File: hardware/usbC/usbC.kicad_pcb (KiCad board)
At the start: 2 copper layers, 27.5 x 25.6 mm, 17 parts, among them J2 Conn_01x02, J3 Conn_01x02, J4 Conn_01x01, J5 Conn_01x02, J6 Conn_01x01, J7 Conn_01x01, J8 Conn_01x01, J9 Connector, USB-TYPE-C-16P, U1 USBLC6-2SC6, U2 AMS1117-3.3

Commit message: wip
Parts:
- removed J4, J8: Conn_01x01, Connector_PinHeader_1.00mm:PinHeader_1x01_P1.00mm_Vertical
- added J1: Conn_01x02, LIB_S2B-ZR_LF__SN_:S2BZRLFSN, F.Cu at (93.0, 83.0)
- J6, J7: value Conn_01x01 -> Conn_01x02; footprint Connector_PinHeader_1.00mm:PinHeader_1x01_P1.00mm_Vertical -> Connector_PinHeader_2.54mm:PinHeader_1x02_P2.54mm_Vertical
- moved J6 24.7 mm to (119.0, 78.7)
- moved J7 12.5 mm to (103.5, 75.5)
- moved J5 7.07 mm to (100.0, 83.0)
- moved J2 2.23 mm to (94.8, 71.1), turned to 180 degrees
- moved C18 1.58 mm to (100.0, 68.3), turned to 90 degrees
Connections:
- F1 pad 1: Net-(F1-Pad1) -> Net-(J7-Pin_2)
- J6 pad 1: GND -> /D+
- J9 pad A9B4: Net-(F1-Pad1) -> Net-(J7-Pin_2)
- J9 pad B9A4: Net-(F1-Pad1) -> Net-(J7-Pin_2)
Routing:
- net VCC: track 16.9 -> 38.6 mm
- net Net-(J7-Pin_2): track 0.00 -> 17.6 mm
- net GND: track 60.2 -> 46.9 mm, vias 8 -> 10
- net Net-(F1-Pad1): track 11.4 -> 0.00 mm
- net /D-: track 9.26 -> 16.3 mm
- net /D+: track 13.1 -> 17.2 mm
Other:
- board size 27.5 x 25.6 mm -> 32 x 25.6 mm

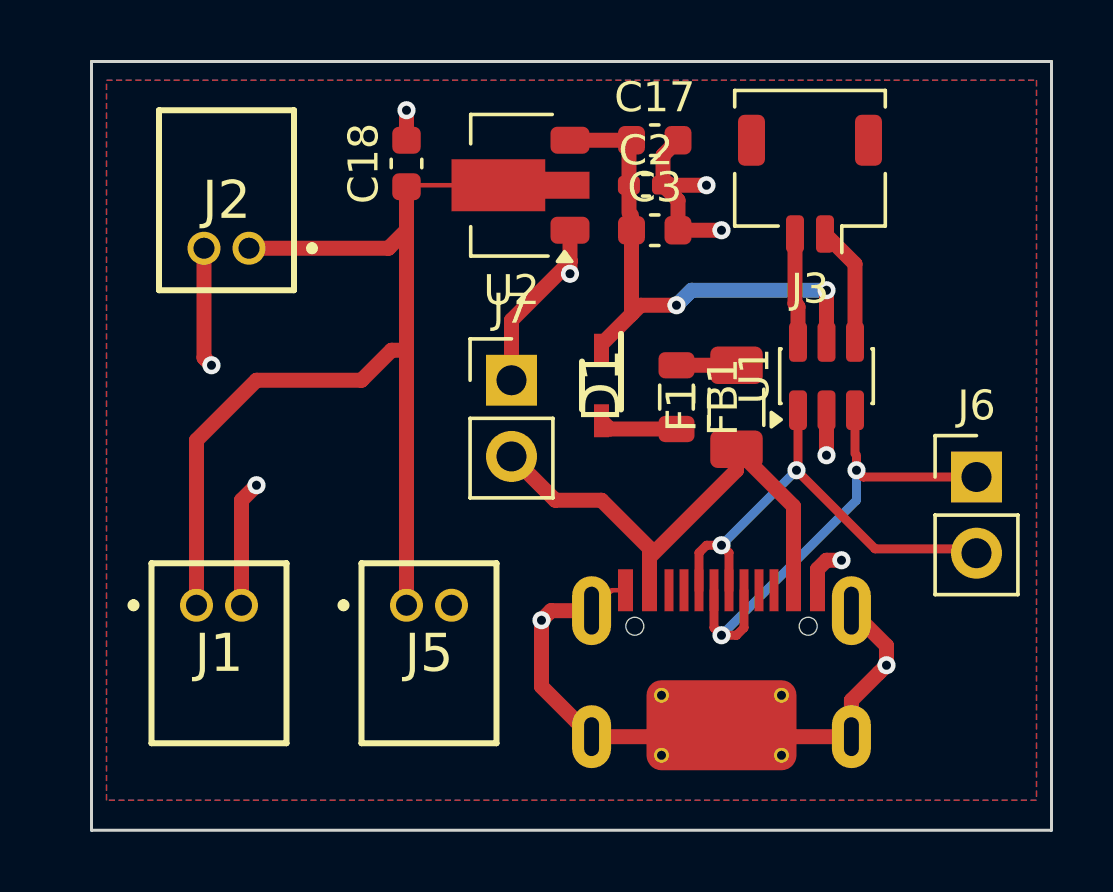
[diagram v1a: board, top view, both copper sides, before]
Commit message: usbc production
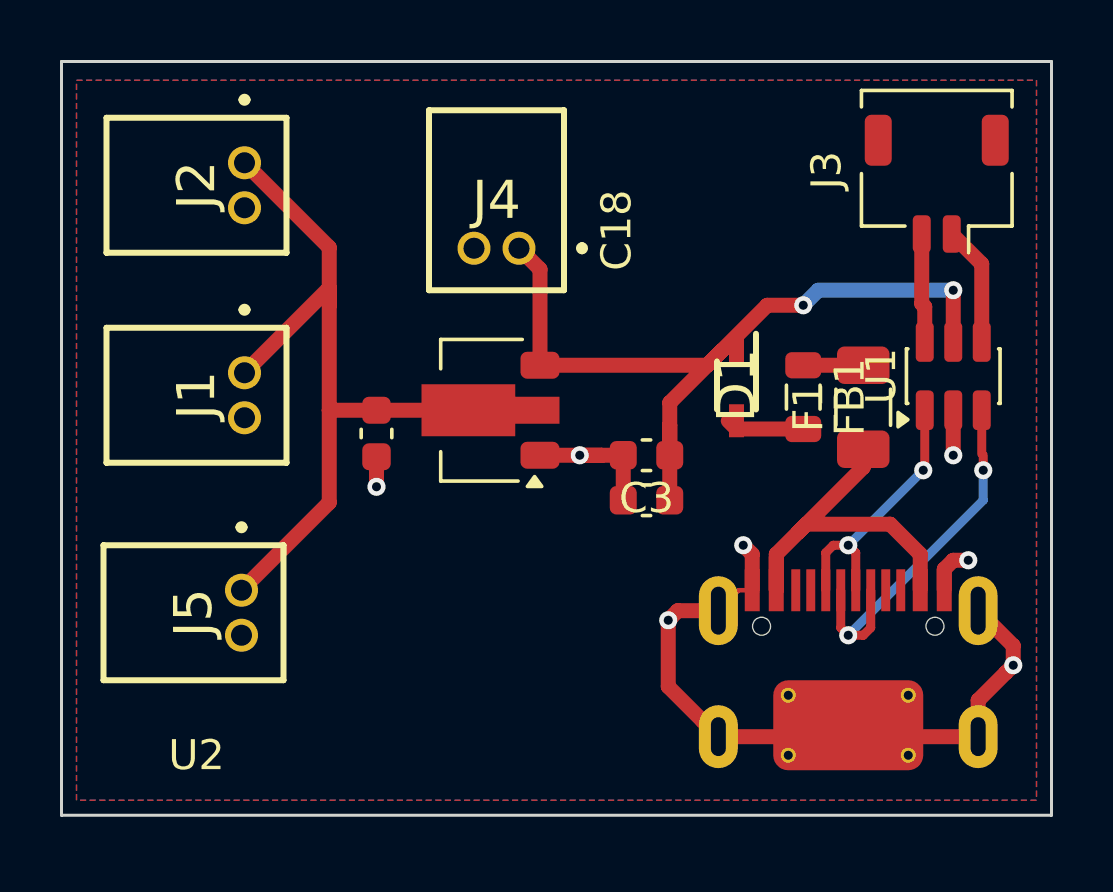
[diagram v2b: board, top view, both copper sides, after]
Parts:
- removed C2: 100n, Capacitor_SMD:C_0402_1005Metric_Pad0.74x0.62mm_HandSolder
- removed J6, J7: Conn_01x02, Connector_PinHeader_2.54mm:PinHeader_1x02_P2.54mm_Vertical
- added J4: Conn_01x02, LIB_S2B-ZR_LF__SN_:S2BZRLFSN, F.Cu at (103.8, 71.1)
- moved C17 12.0 mm to (108.0, 79.5), turned to 180 degrees
- moved C18 9.06 mm to (99.0, 77.3), turned to -90 degrees
- moved J1 7.91 mm to (94.6, 75.2), turned to -90 degrees
- moved U2 7.57 mm to (102.5, 76.5)
- moved C3 7.51 mm to (108.0, 78.0), turned to 180 degrees
- moved J5 5.52 mm to (94.5, 82.5), turned to -90 degrees
- moved D1 4.50 mm to (111.0, 75.7)
- moved F1 4.22 mm to (115.2, 76.4)
- moved FB1 4.22 mm to (113.2, 76.1)
- moved J3 4.22 mm to (117.7, 69.0)
- moved J9 4.22 mm to (114.7, 85.0)
- moved U1 4.22 mm to (118.2, 75.4)
- moved J2 2.85 mm to (94.6, 68.2), turned to -90 degrees
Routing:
- net GND: track 46.9 -> 32.7 mm, vias 10 -> 7
- net VCC: track 38.6 -> 28.2 mm
- net +5V: track 18.1 -> 27.4 mm
- net /D-: track 16.3 -> 9.26 mm
- net Net-(F1-Pad1): track 17.6 -> 12.8 mm
- net /D+: track 17.2 -> 13.1 mm
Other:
- board size 32 x 25.6 mm -> 33 x 25.1 mm
